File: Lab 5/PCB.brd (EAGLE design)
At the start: 104 x 58 mm, 50 parts, among them J1 FTDI_DEVICERA_SMT, M1 WIRELESS-NRF24L01, U2 GY-521MPU6050, U3 MAX7375AXR805-T, U4 ATMEGA328P_TQFP

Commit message: layout update
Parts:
- moved R1 16.3 mm to (11.3, 18.4), turned to 180 degrees
- moved R2 14.5 mm to (11.4, 21.4), turned to 0 degrees
- moved C13 5.32 mm to (26.2, 28.7)
- moved R4 0.71 mm to (26.8, 31.4), turned to 180 degrees
- moved C16 0.50 mm to (26.8, 25.2)
- turned R5 to 180 degrees
- turned R6 to 180 degrees
- turned R7 to 180 degrees

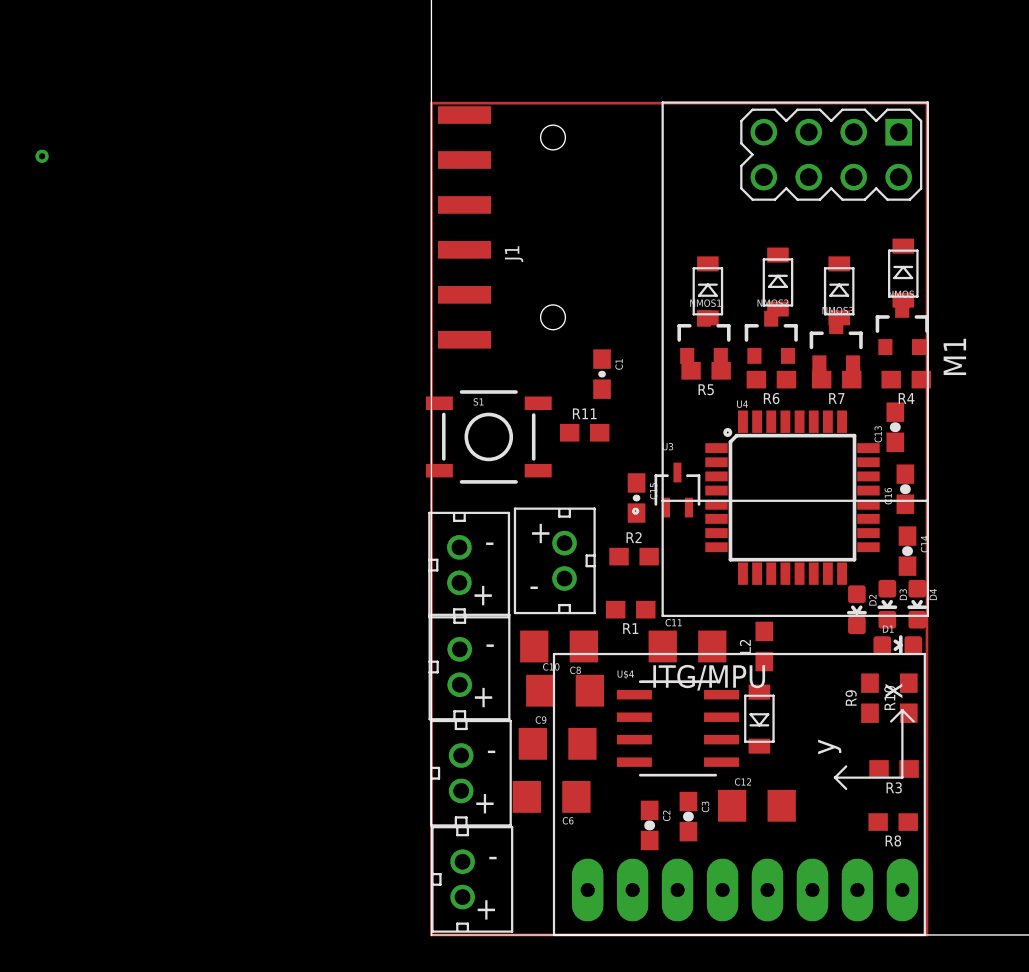
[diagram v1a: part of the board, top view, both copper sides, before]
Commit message: Created a template, things grouped together for easy placement
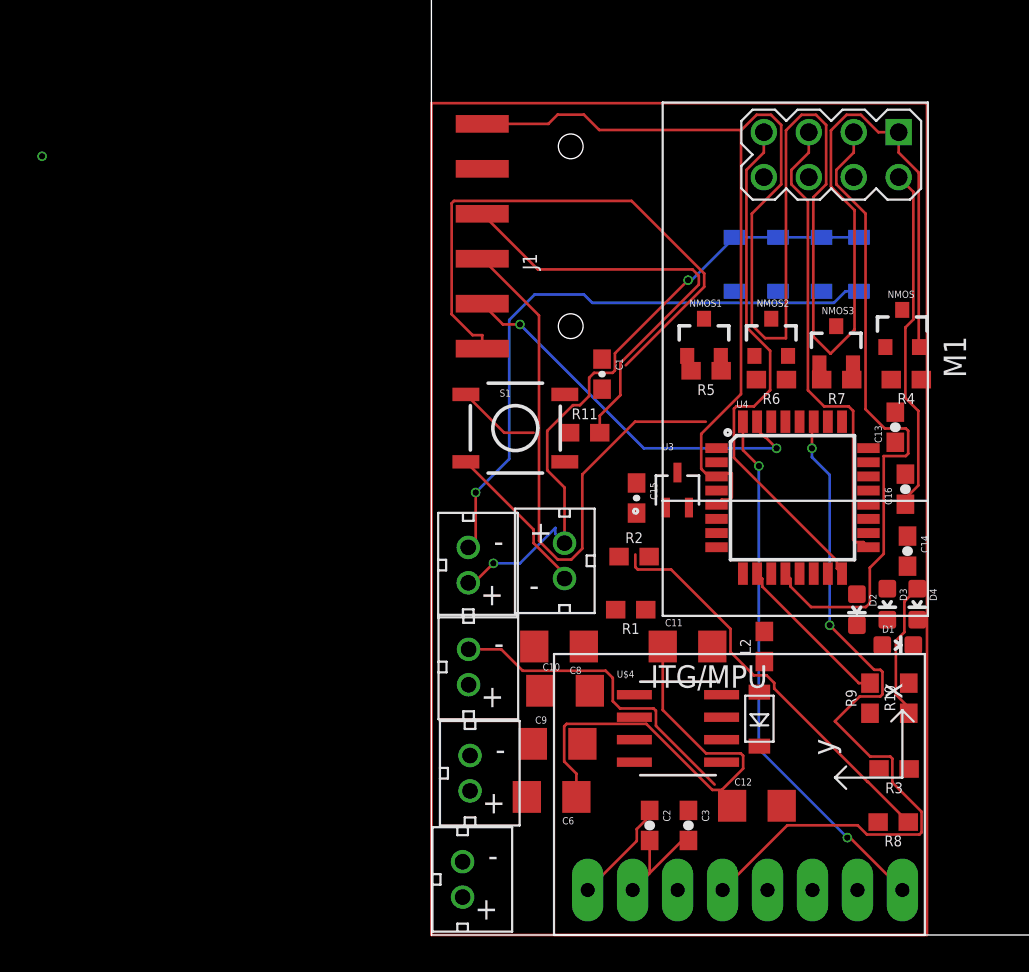
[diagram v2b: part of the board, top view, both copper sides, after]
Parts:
- moved DIODE 2.55 mm to (24.2, 37.9), flipped to the bottom
- moved DIODE1 2.12 mm to (17.1, 37.9), flipped to the bottom
- moved DIODE3 1.80 mm to (22.0, 37.9), flipped to the bottom
- moved S1 1.58 mm to (4.74, 28.6)
- moved J1 1.12 mm to (7.87, 39.5)
- moved DIODE2 1.00 mm to (19.6, 37.9), flipped to the bottom
- moved MOTOR2 0.50 mm to (2.18, 9.14)
- moved C3 0.50 mm to (14.5, 6.19)
- moved MOTOR 0.50 mm to (2.08, 20.9)
- moved MOTOR3 0.50 mm to (2.10, 15.1)
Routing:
- net GND: track 0.00 -> 158.6 mm
- net VCC: track 0.00 -> 50.4 mm
- net IMU-SDA: track 0.00 -> 43.2 mm, vias 0 -> 2
- net BATTERY+: track 0.00 -> 37.7 mm, vias 0 -> 2
- net RF-CE: track 0.00 -> 36.9 mm
- net N$6: track 0.00 -> 34.6 mm, vias 0 -> 1
- net FTDI-RX: track 0.00 -> 32.8 mm
- net N$13: track 0.00 -> 32.3 mm
- net IMU-INT: track 0.00 -> 30.3 mm, vias 0 -> 2
- net RF-MISO: track 0.00 -> 29.9 mm
- net RF-SCK: track 0.00 -> 26.7 mm
- net N$10: track 0.00 -> 23.0 mm
- net FTDI-TX: track 0.00 -> 22.0 mm, vias 0 -> 2
- net N$7: track 0.00 -> 18.3 mm
- net MOTOR3: track 0.00 -> 9.20 mm
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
